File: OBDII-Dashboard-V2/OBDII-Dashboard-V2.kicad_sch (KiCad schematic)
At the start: 26 parts, among them P1 USB_C_Plug_USB2.0, SW1 BOOT, SW2 RESET, U1 LCD, U3 AMS1117-3.3, U4 BME280, U5 ESP32-S3-WROOM-1

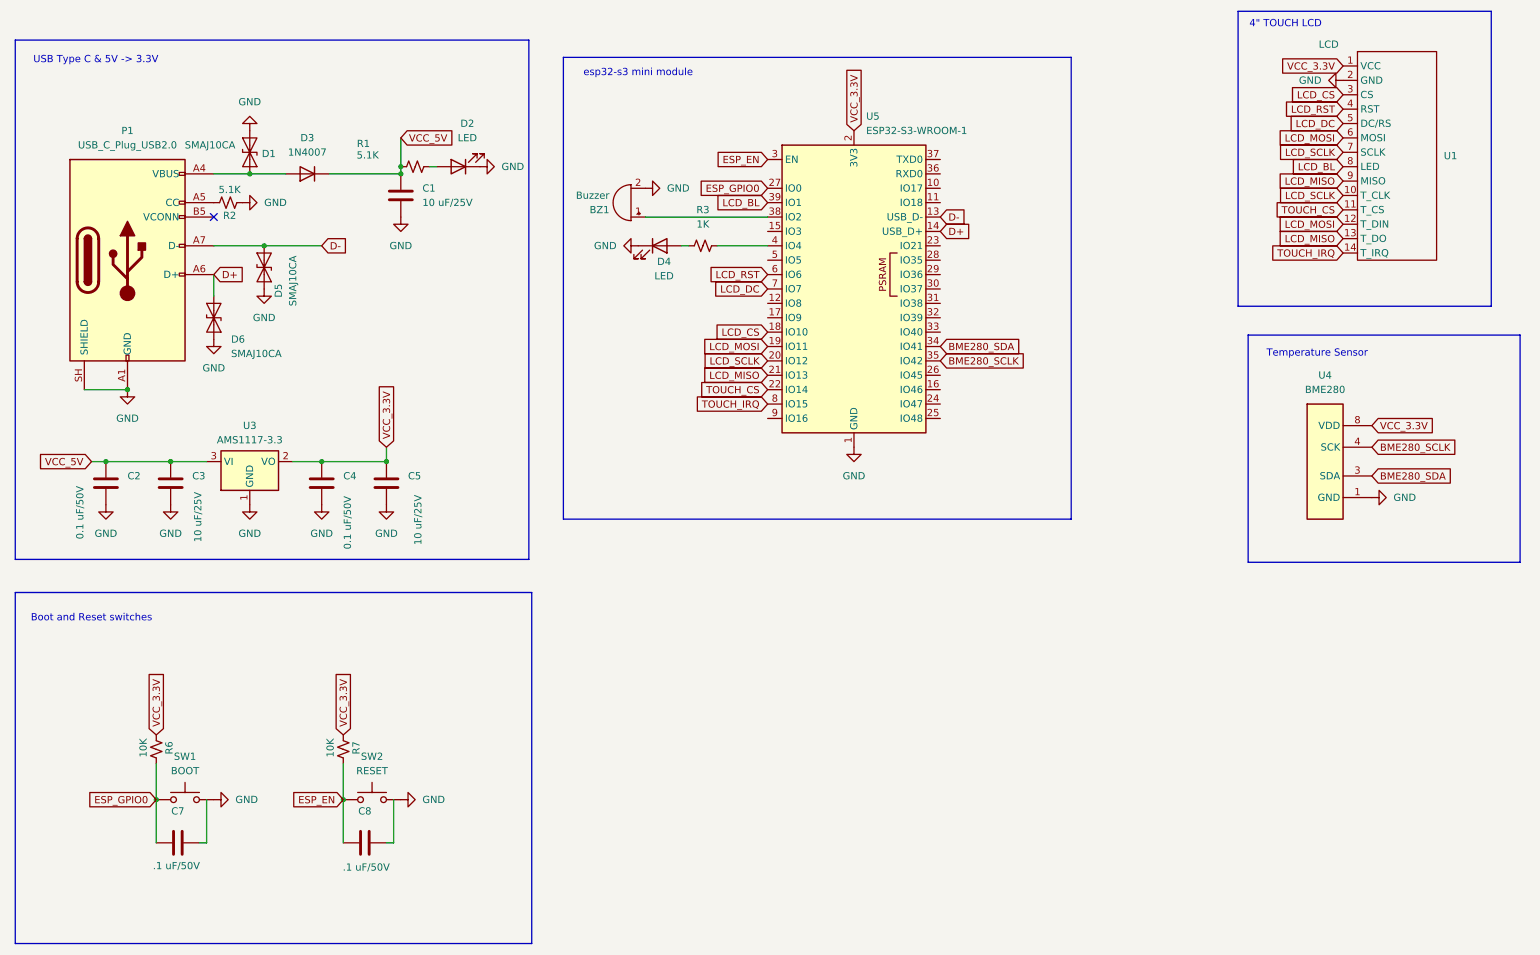
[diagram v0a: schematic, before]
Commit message: updated component placement
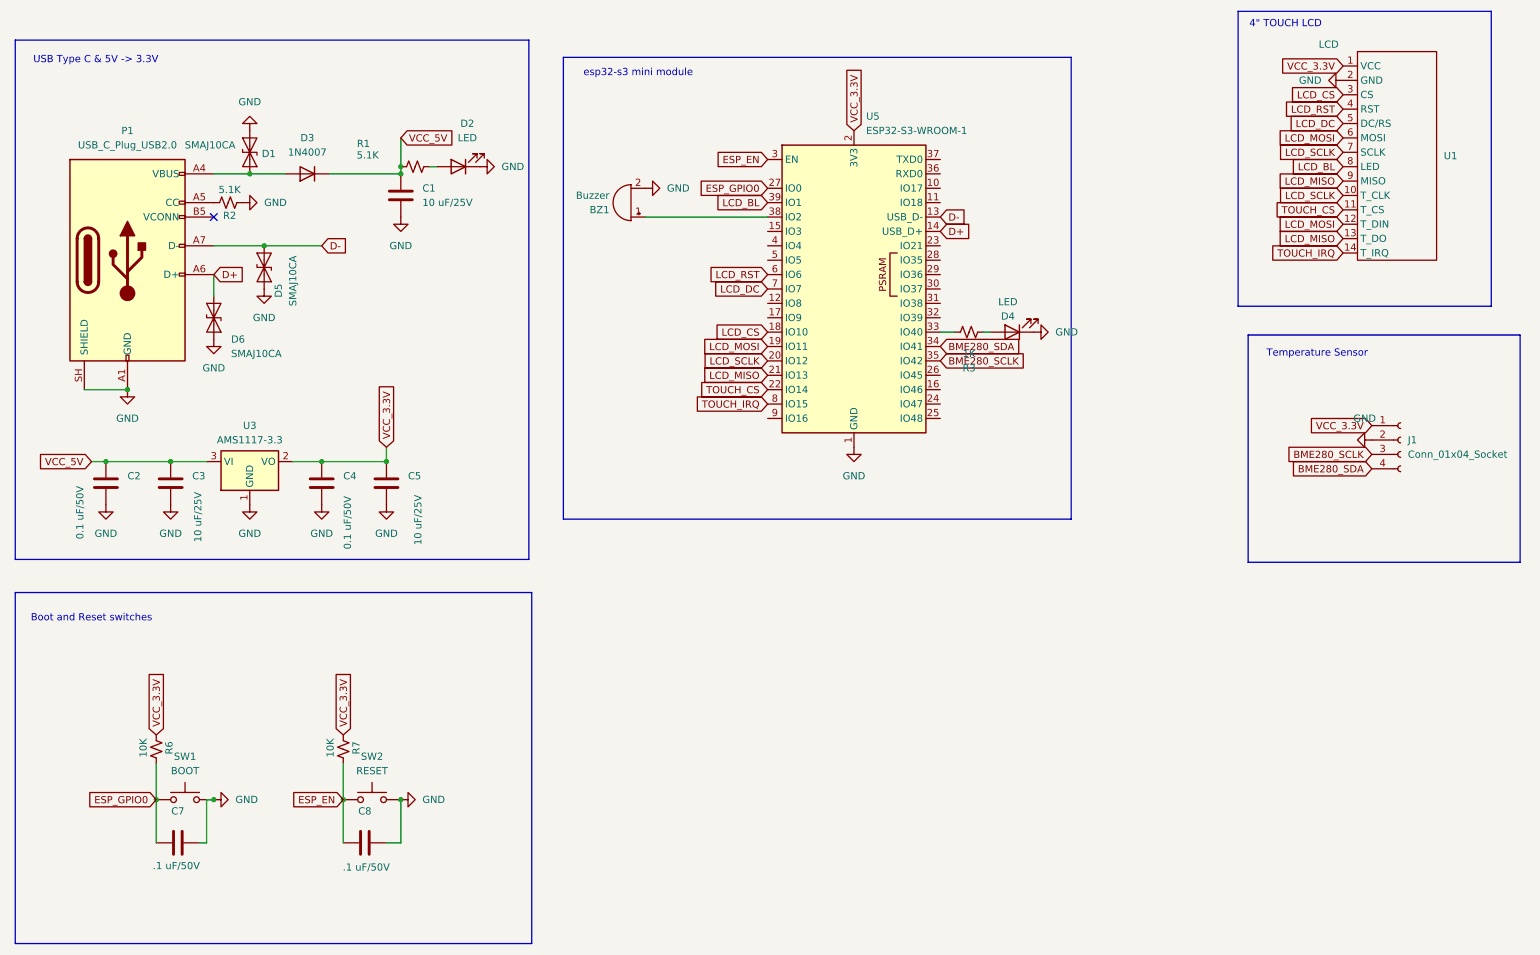
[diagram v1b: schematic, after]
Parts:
- removed U4: BME280, Connector_PinHeader_2.54mm:PinHeader_1x04_P2.54mm_Vertical, symbol OBDII-dashboard:BME280
- added J1: Conn_01x04_Socket, Connector_PinHeader_2.54mm:PinHeader_1x04_P2.54mm_Vertical, symbol Connector:Conn_01x04_Socket
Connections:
- net BME280_SCLK: now also J1.3 (Pin_3)
- net BME280_SDA: now also J1.4 (Pin_4)
- net GND: now also C7.2, C8.2, J1.2 (Pin_2)
- net VCC_3.3V: now also J1.1 (Pin_1)
- net at U5.33 (IO40): now also R3.2
- net at U5.4 (IO4): no longer R3.2
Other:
- moved on the sheet: D4, R3
